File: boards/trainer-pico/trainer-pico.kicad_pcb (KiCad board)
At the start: 2 copper layers, 106.7 x 99.1 mm, 11 parts, among them J1 Conn_01x08_Pin, J10 Conn_01x04_Socket, J2 Conn_01x04_Pin, J3 Conn_01x06_Pin, J4 Conn_01x04_Pin, J5 Conn_01x04_Pin, J6 Conn_01x08_Socket, J7 Conn_01x04_Socket, J8 Conn_01x06_Socket, J9 Conn_01x04_Socket

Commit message: 配線の取り回しを改善
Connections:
- J10 pad 2: /I2C_SCL -> /UART_PICO_RX
- J10 pad 3: /I2C_SDA -> /UART_PICO_TX
- J4 pad 2: /UART_PICO_TX -> /I2C_SDA
- J4 pad 3: /UART_PICO_RX -> /I2C_SCL
- J5 pad 2: /I2C_SCL -> /UART_PICO_RX
- J5 pad 3: /I2C_SDA -> /UART_PICO_TX
- J9 pad 2: /UART_PICO_TX -> /I2C_SDA
- J9 pad 3: /UART_PICO_RX -> /I2C_SCL
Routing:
- net /I2C_SDA: track 65.6 -> 42.7 mm
- net /UART_PICO_TX: track 30.4 -> 50.4 mm
- net /I2C_SCL: track 61.0 -> 42.7 mm
- net /UART_PICO_RX: track 35.0 -> 50.4 mm
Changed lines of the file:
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@@
 			(layers "*.Cu" "*.Mask")
 			(remove_unused_layers no)
-			(net 21 "/UART_PICO_TX")
+			(net 19 "/I2C_SDA")
 			(pinfunction "Pin_2")
 			(pintype "passive")
@@
 			(layers "*.Cu" "*.Mask")
 			(remove_unused_layers no)
-			(net 20 "/UART_PICO_RX")
+			(net 18 "/I2C_SCL")
 			(pinfunction "Pin_3")
 			(pintype "passive")
@@
 			(layers "*.Cu" "*.Mask")
 			(remove_unused_layers no)
-			(net 18 "/I2C_SCL")
+			(net 20 "/UART_PICO_RX")
 			(pinfunction "Pin_2")
 			(pintype "passive")
@@
 			(layers "*.Cu" "*.Mask")
 			(remove_unused_layers no)
-			(net 19 "/I2C_SDA")
+			(net 21 "/UART_PICO_TX")
 			(pinfunction "Pin_3")
 			(pintype "passive")
@@
 			(layers "*.Cu" "*.Mask")
 			(remove_unused_layers no)
-			(net 18 "/I2C_SCL")
+			(net 20 "/UART_PICO_RX")
 			(pinfunction "Pin_2")
 			(pintype "passive")
@@
 			(layers "*.Cu" "*.Mask")
 			(remove_unused_layers no)
-			(net 19 "/I2C_SDA")
+			(net 21 "/UART_PICO_TX")
 			(pinfunction "Pin_3")
 			(pintype "passive")
@@
 			(at 0 9.95 0)
 			(layer "F.Fab")
+			(hide yes)
 			(effects
 				(font
@@
 			(layers "*.Cu" "*.Mask")
 			(remove_unused_layers no)
-			(net 21 "/UART_PICO_TX")
+			(net 19 "/I2C_SDA")
 			(pinfunction "Pin_2")
 			(pintype "passive")
@@
 			(layers "*.Cu" "*.Mask")
 			(remove_unused_layers no)
-			(net 20 "/UART_PICO_RX")
+			(net 18 "/I2C_SCL")
 			(pinfunction "Pin_3")
 			(pintype "passive")
@@
 			)
 		)
-		(fp_text user "${REFERENCE}"
-			(at 0 24.13 0)
-			(unlocked yes)
-			(layer "F.Fab")
-			(effects
-				(font
-					(size 1 1)
-					(thickness 0.15)
-				)
-			)
-		)
 		(pad "1" thru_hole circle
 			(at -8.89 -20.32)
@@
 	)
 	(gr_text "SCL"
-		(at 115.57 121.92 0)
+		(at 115.57 106.68 0)
 		(layer "F.SilkS")
 		(effects
@@
 	)
 	(gr_text "RX"
-		(at 115.57 106.68 0)
+		(at 115.57 121.92 0)
 		(layer "F.SilkS")
 		(effects
@@
 	)
 	(gr_text "→"
-		(at 121.92 121.92 0)
+		(at 121.92 106.68 0)
 		(layer "F.SilkS")
 		(effects
@@
 	)
 	(gr_text "←"
-		(at 121.92 106.68 0)
+		(at 121.92 121.92 0)
 		(layer "F.SilkS")
 		(effects
@@
 	)
 	(gr_text "TX"
-		(at 115.57 104.14 0)
+		(at 115.57 124.46 0)
 		(layer "F.SilkS")
 		(effects
@@
 	)
 	(gr_text "→"
-		(at 121.92 104.14 0)
+		(at 121.92 124.46 0)
 		(layer "F.SilkS")
 		(effects
@@
 	)
 	(gr_text "SDA"
-		(at 115.57 124.46 0)
+		(at 115.57 104.14 0)
 		(layer "F.SilkS")
 		(effects
@@
 	)
 	(gr_text "↔"
-		(at 121.92 124.46 0)
+		(at 121.92 104.14 0)
 		(layer "F.SilkS")
 		(effects
@@
 	)
 	(segment
-		(start 92.71 106.68)
-		(end 92.71 87.63)
+		(start 111.76 106.68)
+		(end 109.22 106.68)
 		(width 0.381)
 		(layer "F.Cu")
@@
 	)
 	(segment
-		(start 119.38 121.92)
-		(end 111.76 121.92)
+		(start 106.68 104.14)
+		(end 106.68 83.82)
 		(width 0.381)
 		(layer "F.Cu")
@@
 	)
 	(segment
-		(start 92.71 87.63)
+		(start 104.14 81.28)
 		(end 99.06 81.28)
 		(width 0.381)
@@
 	)
 	(segment
-		(start 111.76 121.92)
-		(end 107.95 121.92)
+		(start 109.22 106.68)
+		(end 106.68 104.14)
 		(width 0.381)
 		(layer "F.Cu")
@@
 	)
 	(segment
-		(start 107.95 121.92)
-		(end 92.71 106.68)
+		(start 106.68 83.82)
+		(end 104.14 81.28)
 		(width 0.381)
 		(layer "F.Cu")
@@
 	)
 	(segment
-		(start 111.76 124.46)
-		(end 109.668342 124.46)
+		(start 119.38 106.68)
+		(end 111.76 106.68)
+		(width 0.381)
+		(layer "F.Cu")
+		(net 18)
+	)
+	(segment
+		(start 111.76 104.14)
+		(end 119.38 104.14)
 		(width 0.381)
 		(layer "F.Cu")
@@
 	)
 	(segment
-		(start 119.38 124.46)
-		(end 111.76 124.46)
+		(start 107.95 102.87)
+		(end 107.95 82.55)
 		(width 0.381)
 		(layer "F.Cu")
@@
 	)
 	(segment
-		(start 92.129 106.920658)
-		(end 92.129 85.671)
+		(start 107.95 82.55)
+		(end 104.14 78.74)
 		(width 0.381)
 		(layer "F.Cu")
@@
 	)
 	(segment
-		(start 92.129 85.671)
+		(start 104.14 78.74)
 		(end 99.06 78.74)
 		(width 0.381)
@@
 	)
 	(segment
-		(start 109.668342 124.46)
-		(end 92.129 106.920658)
+		(start 111.76 104.14)
+		(end 109.22 104.14)
 		(width 0.381)
 		(layer "F.Cu")
@@
 	)
 	(segment
-		(start 97.209 90.751)
+		(start 109.22 104.14)
+		(end 107.95 102.87)
+		(width 0.381)
+		(layer "F.Cu")
+		(net 19)
+	)
+	(segment
+		(start 107.95 121.92)
+		(end 105.41 119.38)
+		(width 0.381)
+		(layer "F.Cu")
+		(net 20)
+	)
+	(segment
+		(start 102.87 88.9)
 		(end 99.06 88.9)
 		(width 0.381)
@@
 	)
 	(segment
-		(start 97.209 96.984829)
-		(end 97.209 90.751)
+		(start 105.41 91.44)
+		(end 102.87 88.9)
 		(width 0.381)
 		(layer "F.Cu")
@@
 	)
 	(segment
-		(start 106.904171 106.68)
-		(end 97.209 96.984829)
+		(start 111.76 121.92)
+		(end 107.95 121.92)
 		(width 0.381)
 		(layer "F.Cu")
@@
 	)
 	(segment
-		(start 111.76 106.68)
-		(end 106.904171 106.68)
+		(start 119.38 121.92)
+		(end 111.76 121.92)
 		(width 0.381)
 		(layer "F.Cu")
@@
 	)
 	(segment
-		(start 119.38 106.68)
-		(end 111.76 106.68)
+		(start 105.41 119.38)
+		(end 105.41 91.44)
 		(width 0.381)
 		(layer "F.Cu")
@@
 	)
 	(segment
-		(start 111.76 104.14)
-		(end 105.41 104.14)
+		(start 104.14 120.65)
+		(end 107.95 124.46)
 		(width 0.381)
 		(layer "F.Cu")
@@
 	)
 	(segment
-		(start 111.76 104.14)
-		(end 119.38 104.14)
+		(start 107.95 124.46)
+		(end 111.76 124.46)
 		(width 0.381)
 		(layer "F.Cu")
@@
 	)
 	(segment
-		(start 105.41 104.14)
-		(end 97.79 96.52)
+		(start 99.06 91.44)
+		(end 102.87 91.44)
 		(width 0.381)
 		(layer "F.Cu")
@@
 	)
 	(segment
-		(start 97.79 96.52)
-		(end 97.79 92.71)
+		(start 104.14 92.71)
+		(end 104.14 120.65)
+		(width 0.381)
+		(layer "F.Cu")
+		(net 21)
+	)
+	(segment
+		(start 119.38 124.46)
+		(end 111.76 124.46)
 		(width 0.381)
 		(layer "F.Cu")
@@
 	)
 	(segment
-		(start 97.79 92.71)
-		(end 99.06 91.44)
+		(start 102.87 91.44)
+		(end 104.14 92.71)
 		(width 0.381)
 		(layer "F.Cu")

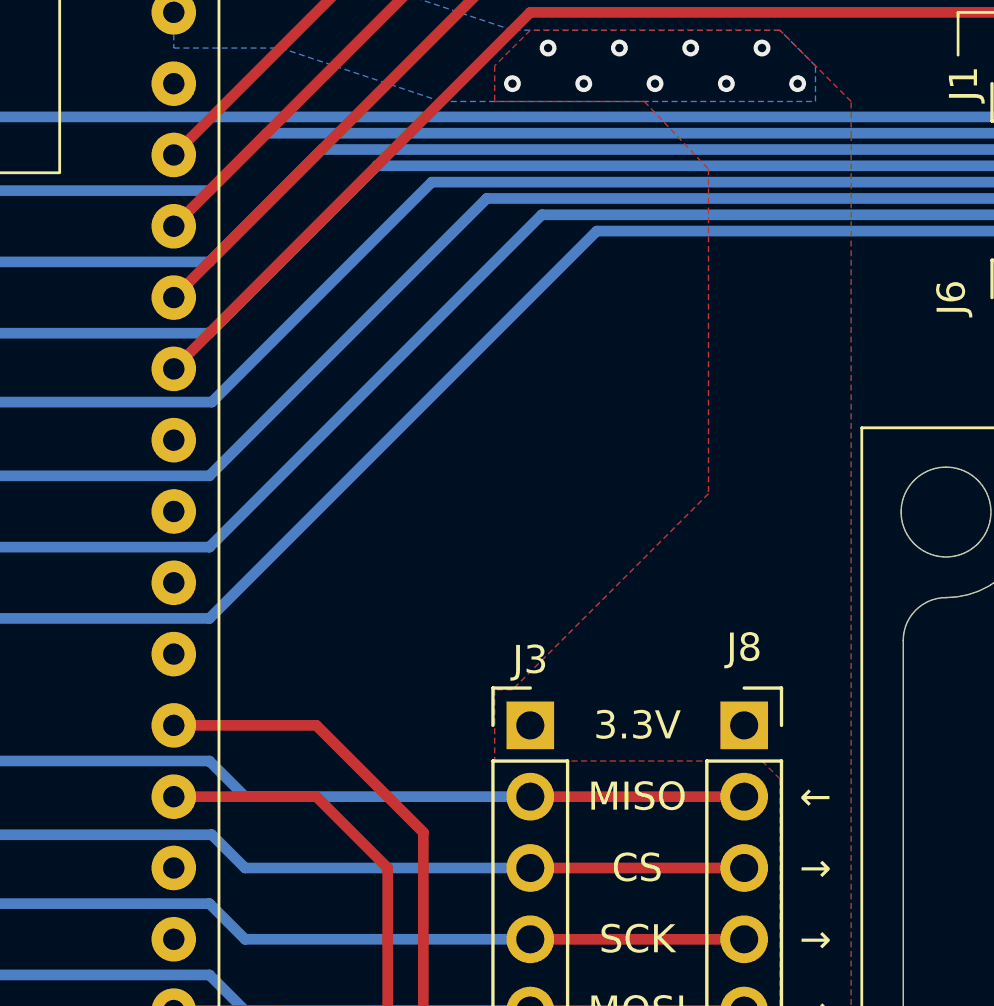
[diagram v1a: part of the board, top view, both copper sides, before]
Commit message: I2C の外部プルアップ用の回路を追加
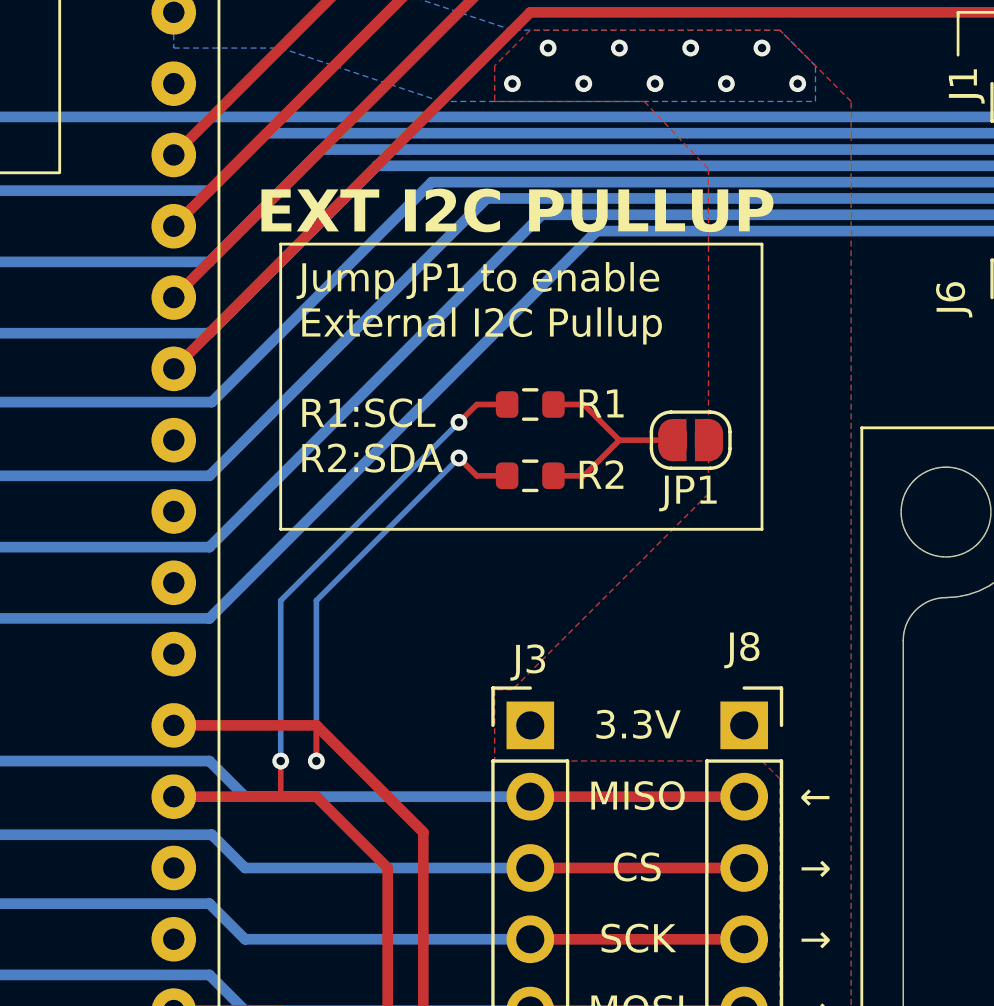
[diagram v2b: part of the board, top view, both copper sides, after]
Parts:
- added JP1: Jumper_2_Open, Jumper:SolderJumper-2_P1.3mm_Open_RoundedPad1.0x1.5mm, F.Cu at (117.5, 68.6)
- added R1: R, Resistor_SMD:R_0603_1608Metric, F.Cu at (111.8, 67.3)
- added R2: R, Resistor_SMD:R_0603_1608Metric, F.Cu at (111.8, 69.8)
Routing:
- net /I2C_SCL: track 42.7 -> 60.7 mm, vias 0 -> 2
- net /I2C_SDA: track 42.7 -> 58.9 mm, vias 0 -> 2
- net Net-(JP1-B): track 0.00 -> 7.64 mm
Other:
- board text added: "EXT I2C PULLUP"
- board text added: "Jump JP1 to enable External I2C Pullup R1:SCL R2:SDA"

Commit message: 電源パターンを調整
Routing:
- net GND: track 0.00 -> 1.91 mm, vias 0 -> 9
- net /GP_0: track 56.9 -> 58.6 mm
- net /ADC_2: track 76.3 -> 78.0 mm
- net /ADC_3: track 78.3 -> 79.9 mm
- net /ADC_0: track 72.4 -> 73.9 mm
- net /ADC_1: track 74.4 -> 75.9 mm
- net /I2C_SDA: track 58.9 -> 59.6 mm
- net /I2C_SCL: track 60.7 -> 61.4 mm
- net +3.3V: vias 9 -> 7

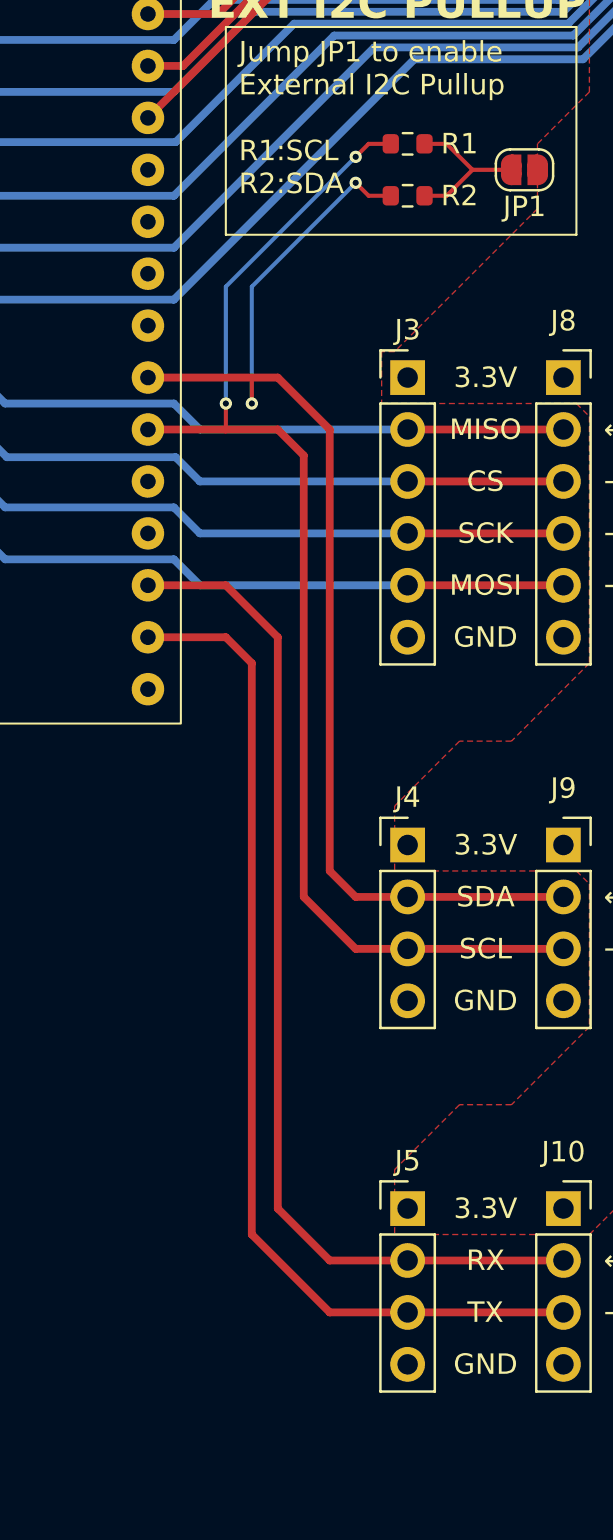
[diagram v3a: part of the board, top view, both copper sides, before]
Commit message: シルクの刻印をいい感じにした
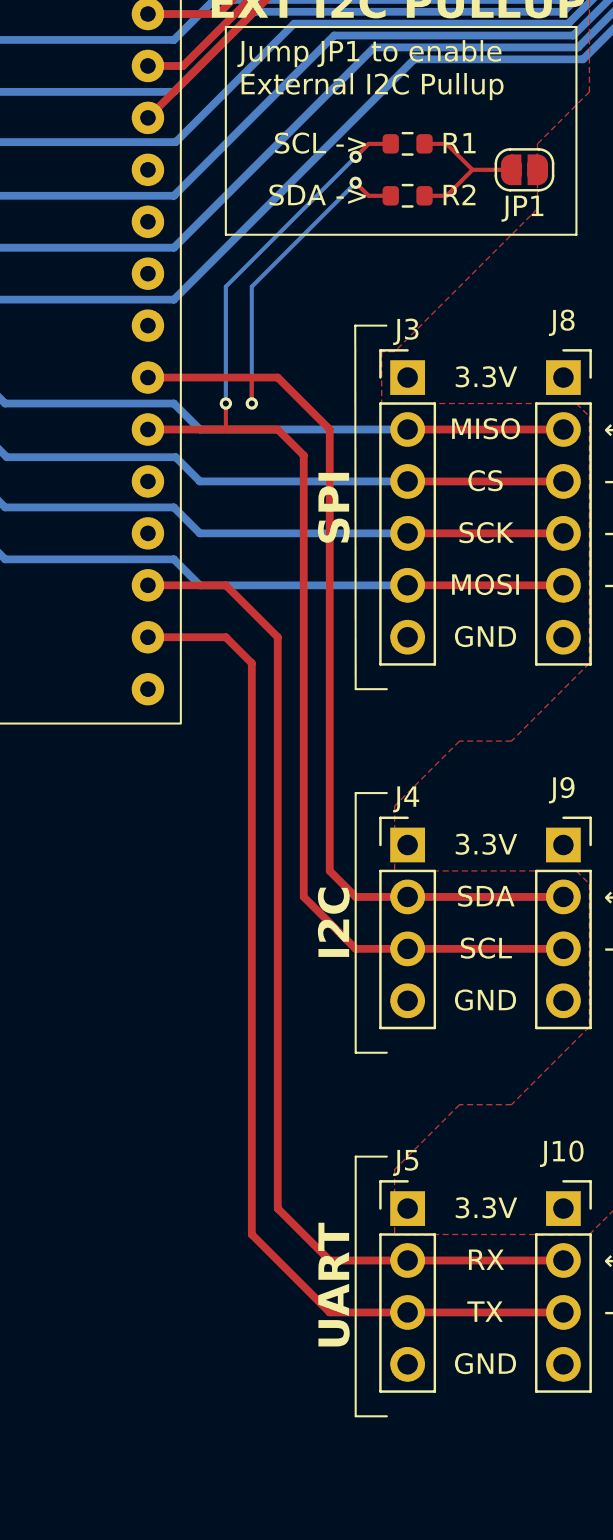
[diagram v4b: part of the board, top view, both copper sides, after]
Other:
- board text added: "I2C"
- board text added: "Jump JP1 to enable External I2C Pullup"
- board text added: "SCL ->"
- board text added: "SDA ->"
- board text added: "SPI"
- board text added: "UART"
- board text removed: "Jump JP1 to enable External I2C Pullup R1:SCL R2:SDA"

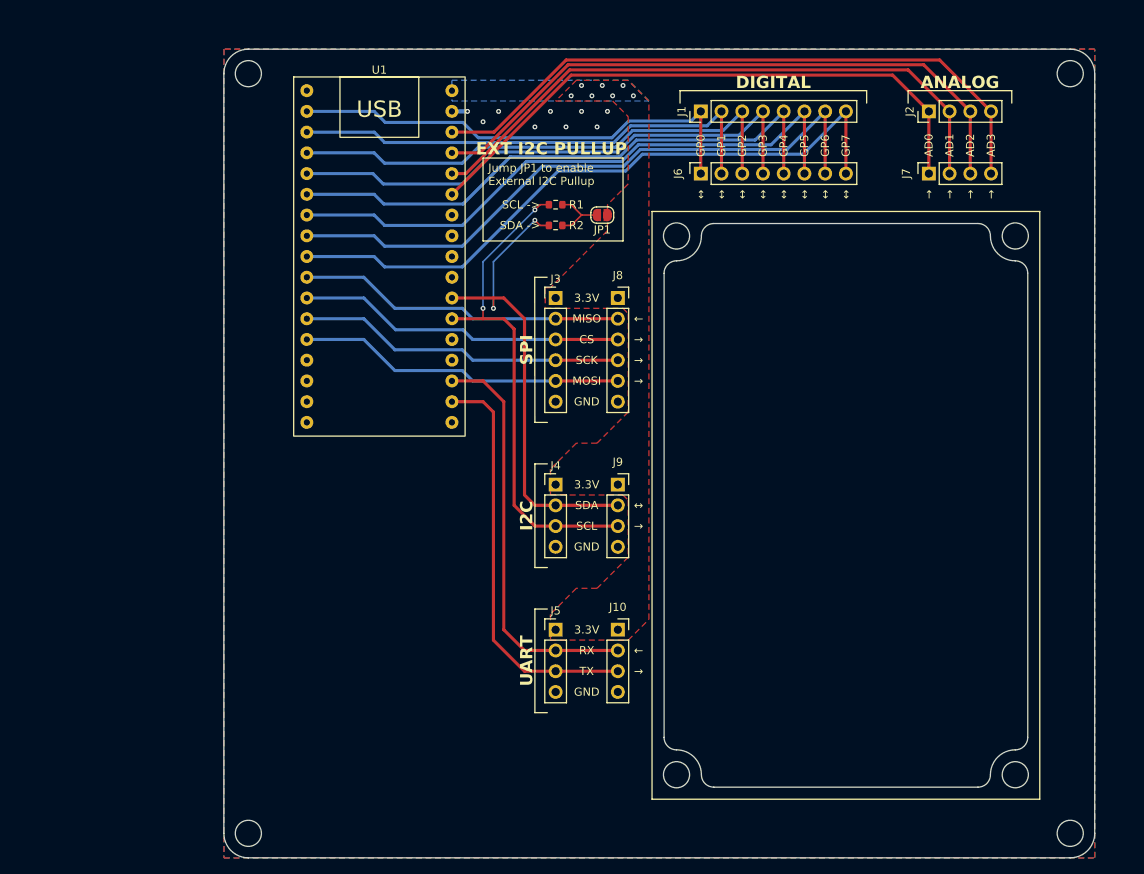
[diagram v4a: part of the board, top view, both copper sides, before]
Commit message: Pico の両側にピンソケット・ピンヘッダを追加
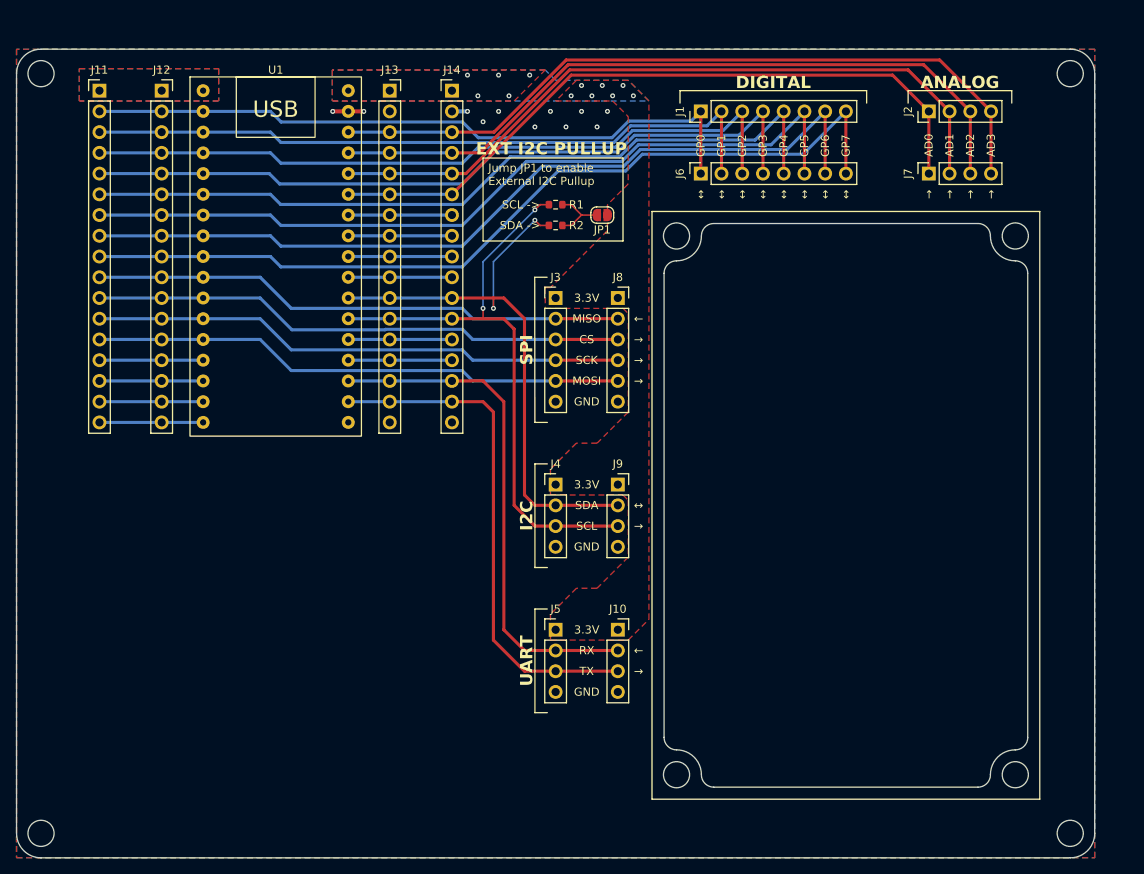
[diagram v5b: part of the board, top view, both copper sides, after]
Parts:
- added J11: Conn_01x17_Pin, Connector_PinHeader_2.54mm:PinHeader_1x17_P2.54mm_Vertical, F.Cu at (55.9, 53.3)
- added J12: Conn_01x17_Socket, Connector_PinSocket_2.54mm:PinSocket_1x17_P2.54mm_Vertical, F.Cu at (63.5, 53.3)
- added J13: Conn_01x17_Socket, Connector_PinSocket_2.54mm:PinSocket_1x17_P2.54mm_Vertical, F.Cu at (91.4, 53.3)
- added J14: Conn_01x17_Pin, Connector_PinHeader_2.54mm:PinHeader_1x17_P2.54mm_Vertical, F.Cu at (99.1, 53.3)
- moved U1 12.7 mm to (77.5, 73.7)
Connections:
- U1 pad 14: unconnected-(U1-UART0_TX/I2C0_SDA/SPI1_RX/GP12-Pad14) -> /GP_12
- U1 pad 15: unconnected-(U1-UART0_RX/I2C0_SCL/SPI1_CSn/GP13-Pad15) -> /GP_13
- U1 pad 16: unconnected-(U1-I2C1_SDA/SPI1_SCK/GP14-Pad16) -> /GP_14
- U1 pad 17: unconnected-(U1-I2C1_SCL/SPI1_TX/GP15-Pad17) -> /GP_15
- U1 pad 21: unconnected-(U1-I2C1_SDA/SPI0_SCK/GP18-Pad21) -> /GP_18
- U1 pad 22: unconnected-(U1-I2C1_SCL/SPI0_TX/GP19-Pad22) -> /GP_19
- U1 pad 25: unconnected-(U1-GP22-Pad25) -> /GP_22
- U1 pad 26: unconnected-(U1-GP23-Pad26) -> /GP_23
- U1 pad 27: unconnected-(U1-GP24-Pad27) -> /GP_24
- U1 pad 28: unconnected-(U1-GP25-Pad28) -> /GP_25
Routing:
- net /GP_4: track 71.2 -> 96.7 mm
- net +3.3V: track 40.2 -> 65.7 mm, vias 7 -> 12
- net /SPI_SCK: track 40.2 -> 65.6 mm
- net /SPI_MISO: track 40.2 -> 65.6 mm
- net /GP_7: track 82.1 -> 107.5 mm
- net /GP_6: track 78.5 -> 103.9 mm
- net /GP_5: track 74.9 -> 100.3 mm
- net /SPI_MOSI: track 40.2 -> 65.6 mm
- net /GP_2: track 64.1 -> 89.5 mm
- net /GP_1: track 60.5 -> 85.9 mm
- net /GP_0: track 58.6 -> 84.0 mm
- net /GP_3: track 67.7 -> 93.1 mm
- net /UART_PICO_TX: track 50.4 -> 63.1 mm
- net /UART_PICO_RX: track 50.4 -> 63.1 mm
- net /I2C_SCL: track 61.4 -> 74.1 mm
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- added copper zone on B.Cu, net +5V
- added copper zone on F.Cu, net +5V
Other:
- board size 106.7 x 99.1 mm -> 132.1 x 99.1 mm
